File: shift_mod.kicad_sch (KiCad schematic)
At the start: 24 parts, among them J1 Screw_Terminal_01x02, J10 Screw_Terminal_01x02, J11 Screw_Terminal_01x02, J2 Screw_Terminal_01x02, J3 Screw_Terminal_01x02, J4 Screw_Terminal_01x02, J5 Screw_Terminal_01x02, J6 Screw_Terminal_01x02, J7 Screw_Terminal_01x02, J8 Screw_Terminal_01x02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

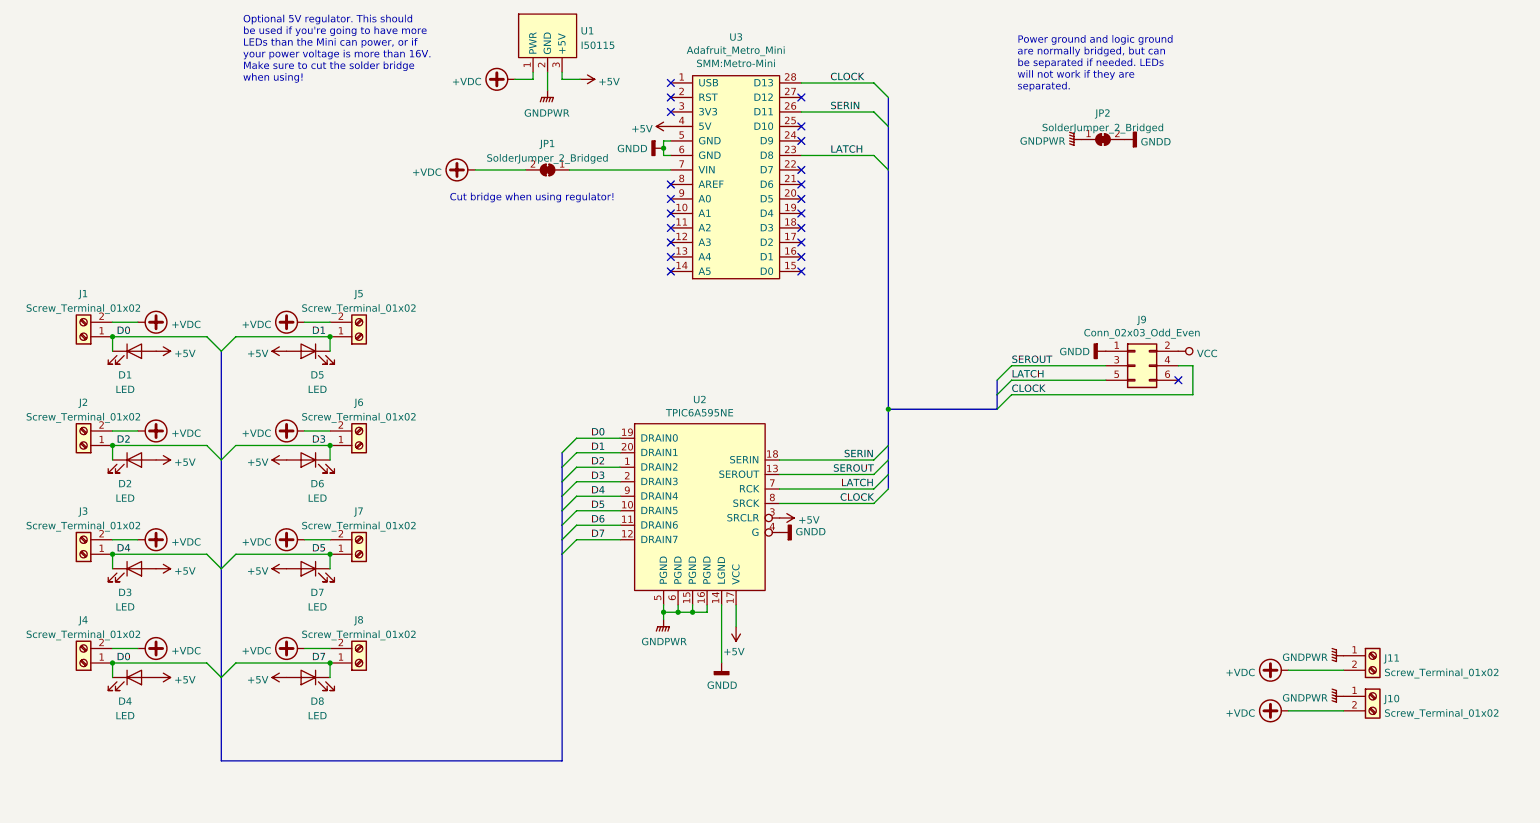
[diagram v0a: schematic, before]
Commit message: add daughter board
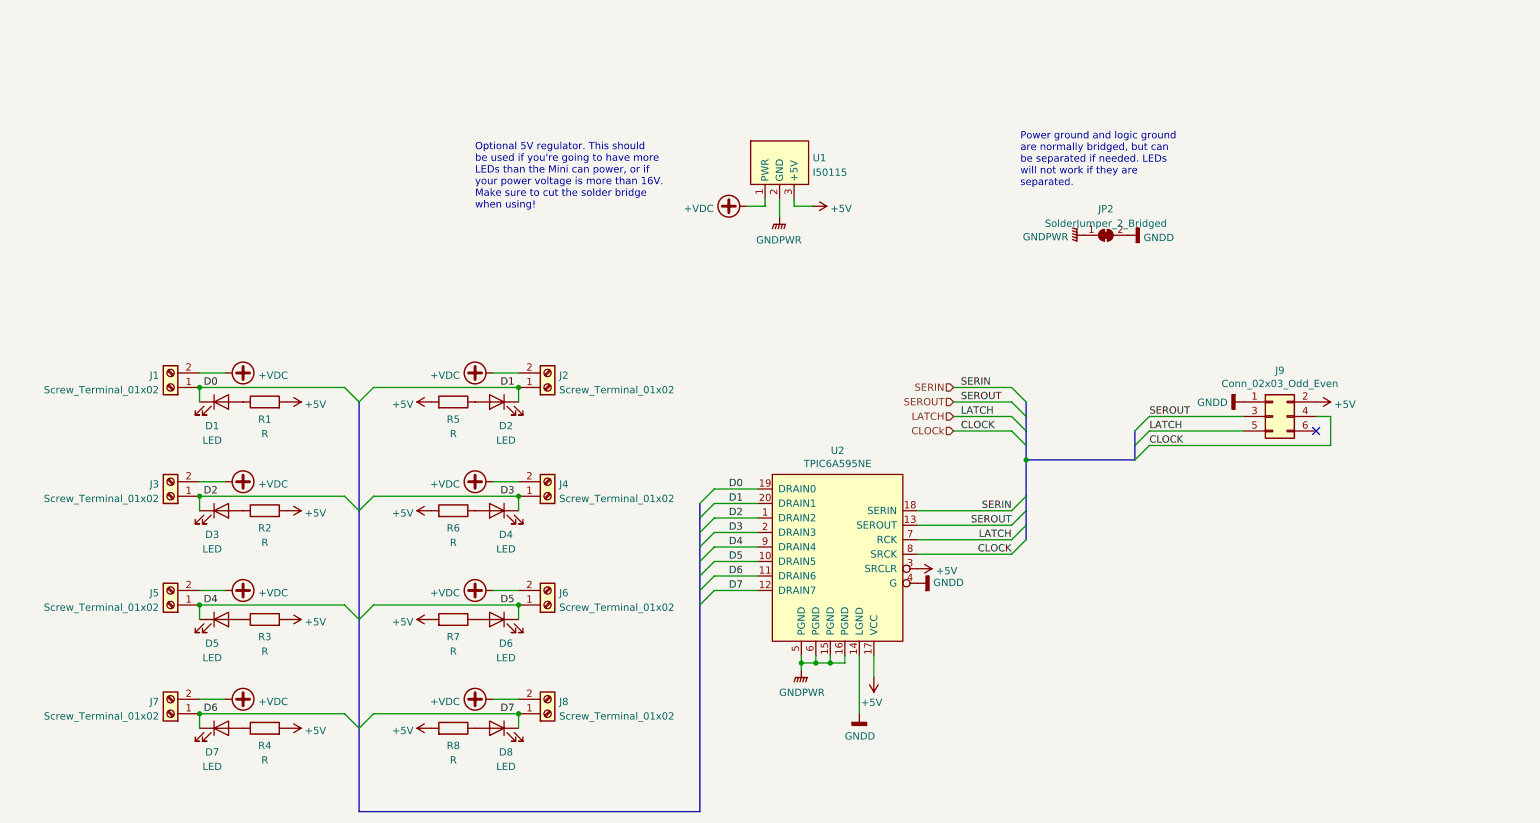
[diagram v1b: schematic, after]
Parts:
- removed D5, D7: LED, LED_THT:LED_D3.0mm, symbol Device:LED
- removed J10, J11, J5, J7: Screw_Terminal_01x02, TerminalBlock:TerminalBlock_bornier-2_P5.08mm, symbol Connector:Screw_Terminal_01x02
- removed JP1: SolderJumper_2_Bridged, Jumper:SolderJumper-2_P1.3mm_Bridged_RoundedPad1.0x1.5mm, symbol Jumper:SolderJumper_2_Bridged
- removed U3: Adafruit_Metro_Mini, SMM:Metro-Mini, symbol SMM:Adafruit_Metro_Mini
- added D2, D4: LED, LED_THT:LED_D3.0mm, symbol Device:LED
- added J2, J4: Screw_Terminal_01x02, TerminalBlock:TerminalBlock_bornier-2_P5.08mm, symbol Connector:Screw_Terminal_01x02
- added R1, R2, R3, R4, R5, R6, R7, R8: R, symbol Device:R
- renumbered D2 to D3, D3 to D5, D4 to D7, J2 to J3, J3 to J5, J4 to J7
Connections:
- net VCC is gone; now on net +5V: J9.2 (Pin_2)
- net +5V: now also R1.2, R2.2, R3.2, R4.2, R5.2, R6.2, R7.2, R8.2; no longer D1.2 (A), D3.2 (A), D5.2 (A), D6.2 (A), D7.2 (A), D8.2 (A)
- net +VDC: now also J2.2 (Pin_2), J4.2 (Pin_2)
- net D0: no longer D7.1 (K), J7.1 (Pin_1)
- net D1: now also D2.1 (K), J2.1 (Pin_1)
- net D3: now also D4.1 (K), J4.1 (Pin_1); no longer D6.1 (K), J6.1 (Pin_1)
- net D5: now also D6.1 (K), J6.1 (Pin_1)
- net D6: now also D7.1 (K), J7.1 (Pin_1)
- net CLOCK renamed CLOCk
- new net: D8.2 (A), R8.1
- new net: D1.2 (A), R1.1
- new net: D4.2 (A), R6.1
- new net: D2.2 (A), R5.1
- new net: D6.2 (A), R7.1
- new net: D5.2 (A), R3.1
- new net: D3.2 (A), R2.1
- new net: D7.2 (A), R4.1
- no-connect marks 22 -> 1
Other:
- note removed: "Cut bridge when using regulator!"
- title: Power Shift Register - Mother Board -> Power Shift Register - Shift Module
- moved on the sheet: D1, D3, D5, D7, J1, J3, J5, J7, J9, JP2, U1, U2
